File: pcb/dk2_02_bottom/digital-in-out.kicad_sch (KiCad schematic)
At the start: 24 parts, among them Q2 MMBT3904, U14 TL072, U15 TL072, U16 TL072

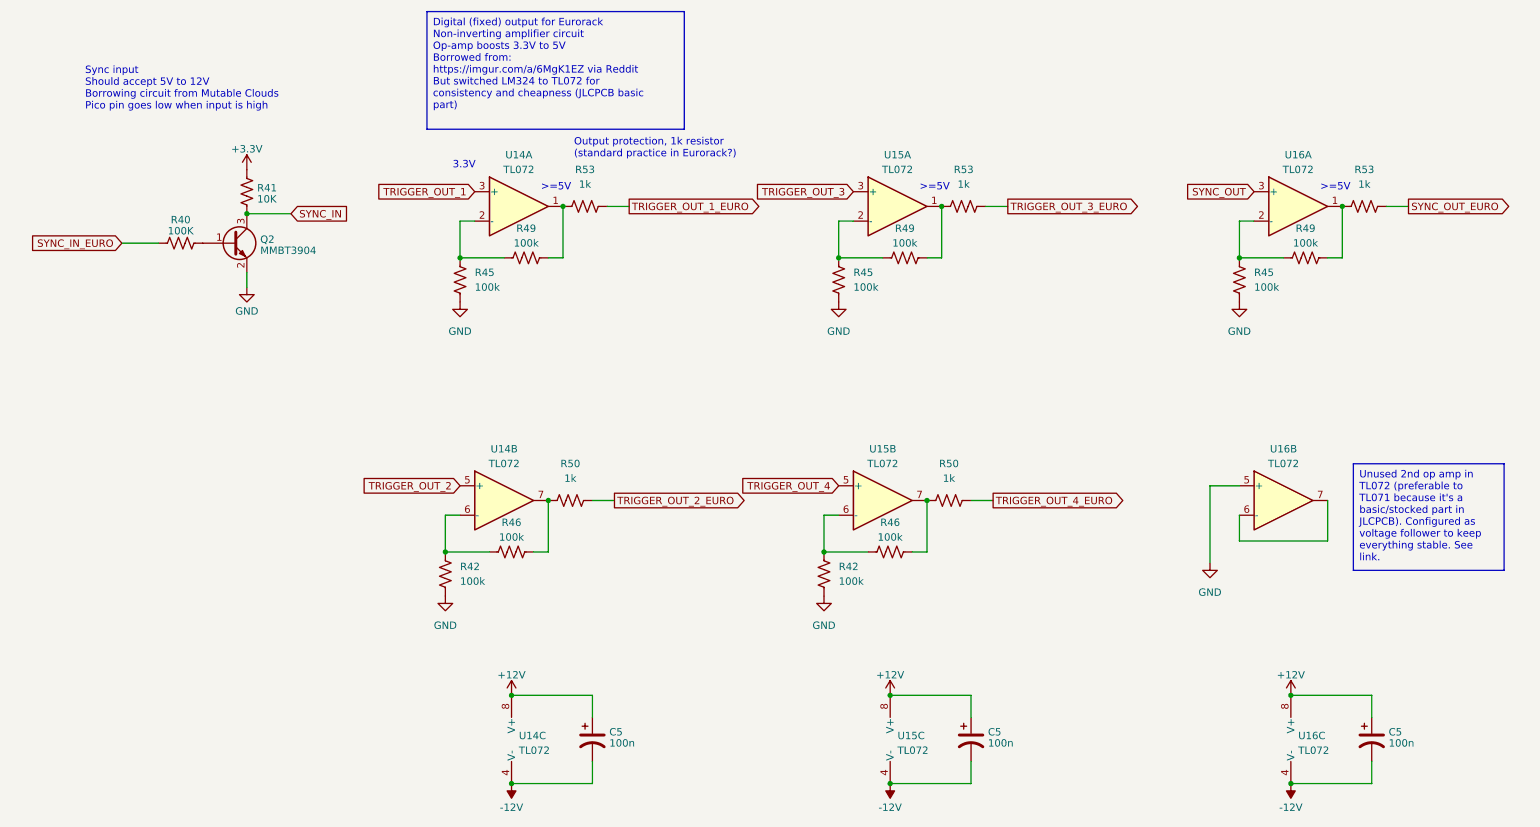
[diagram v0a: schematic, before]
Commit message: bottom pcb looks fairly easy
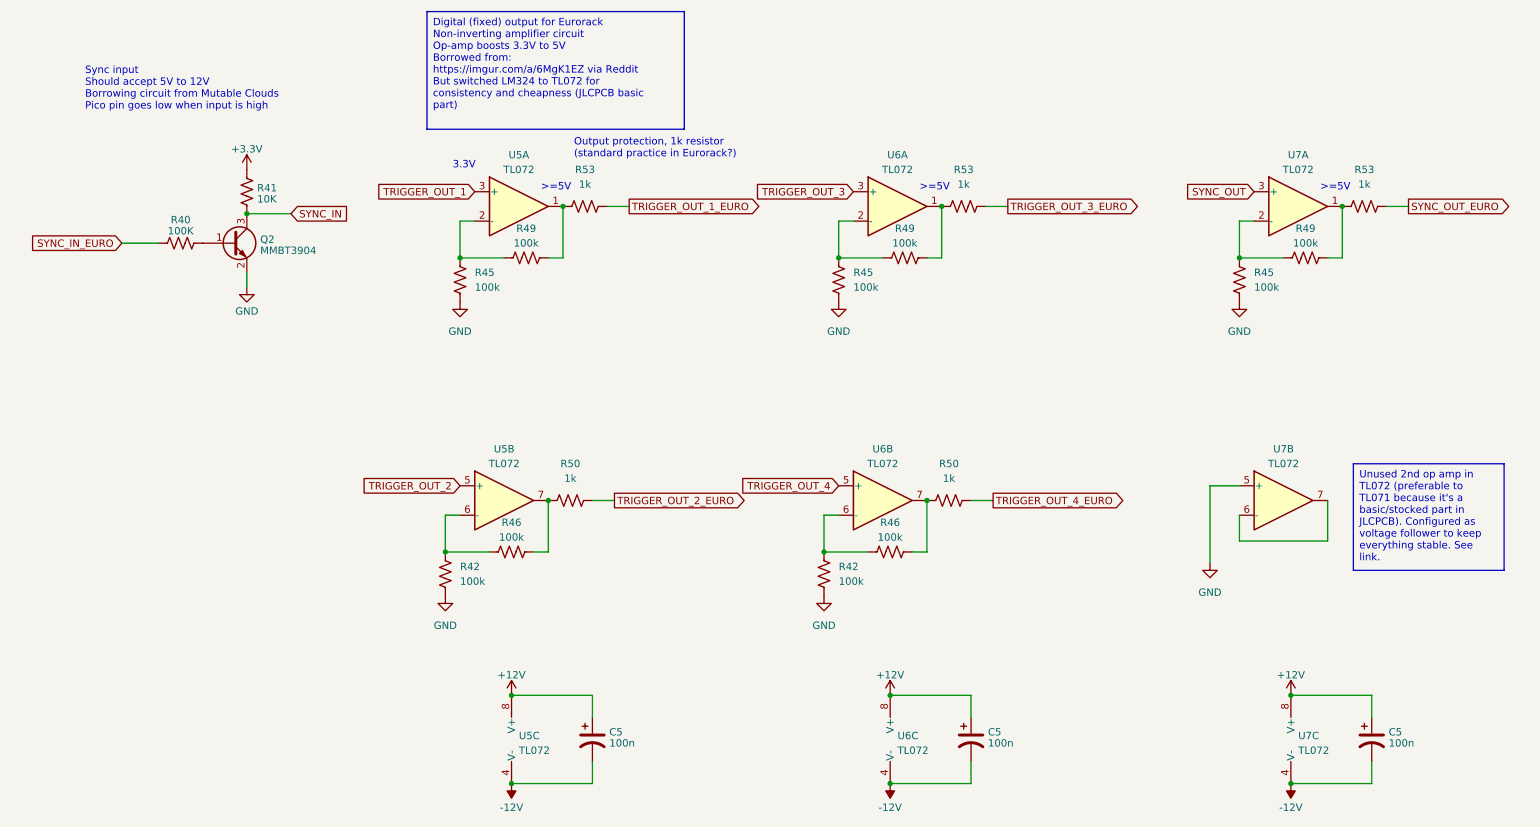
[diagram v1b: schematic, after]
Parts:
- renumbered U14 to U5, U15 to U6, U16 to U7
